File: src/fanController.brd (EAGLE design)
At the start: 41.6 x 36.8 mm, 20 parts, among them Q1 MOSFET-NCHANNELFDD8780

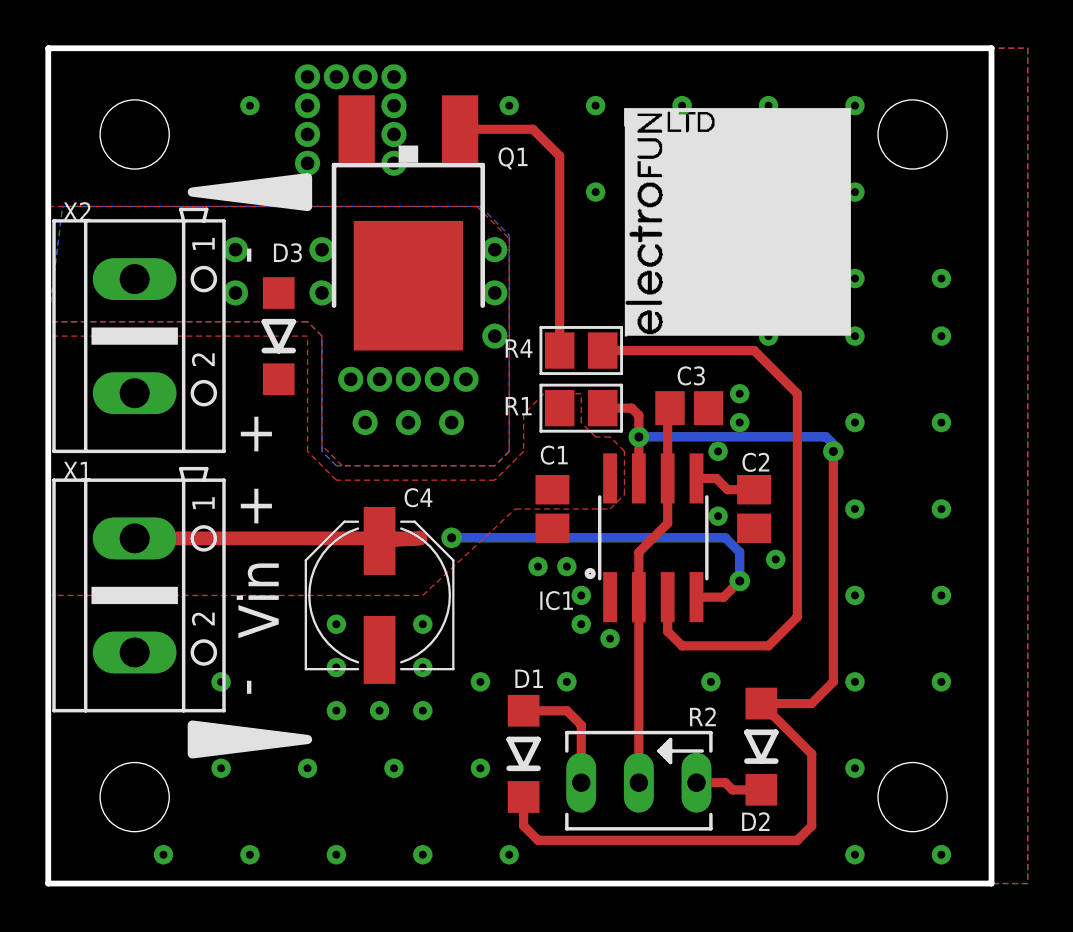
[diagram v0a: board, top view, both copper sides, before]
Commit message: Updated fan controller.
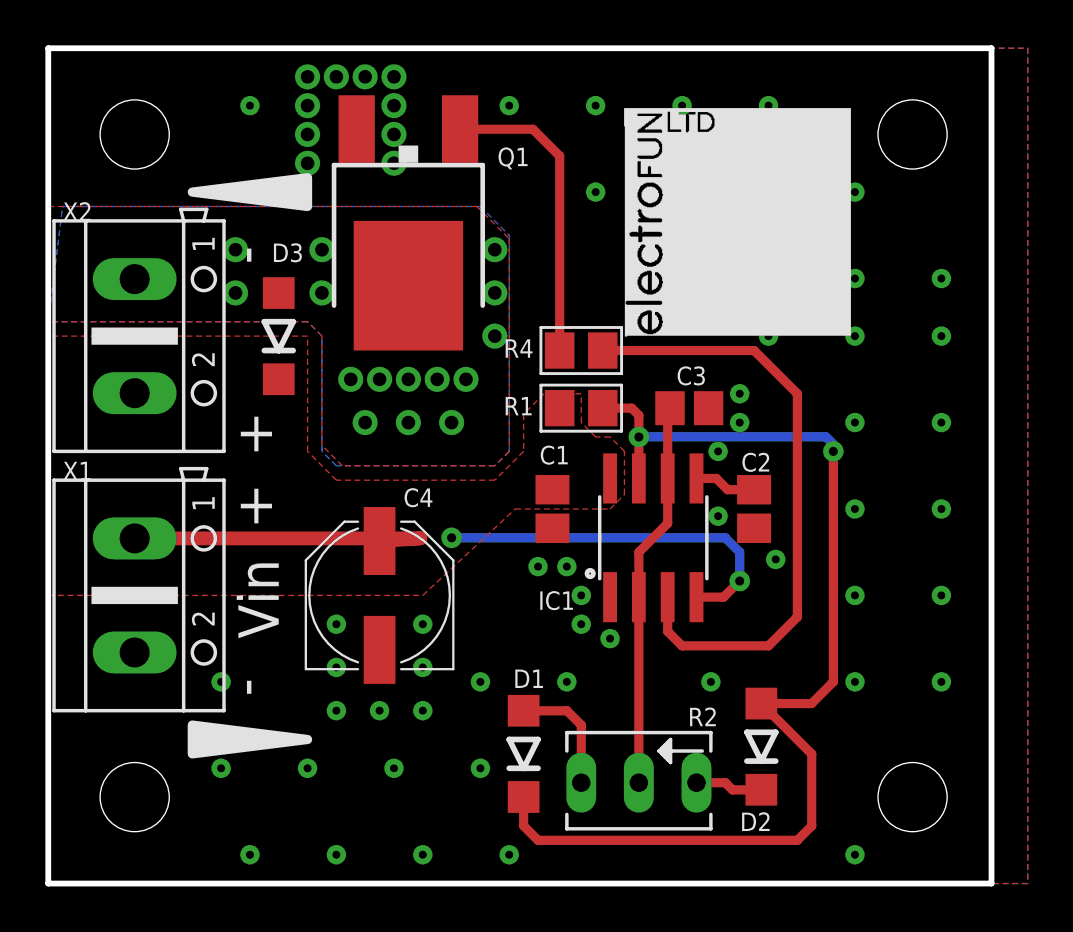
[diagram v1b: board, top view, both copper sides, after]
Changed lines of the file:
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@@
 <layer number="37" name="tTest" color="7" fill="1" visible="no" active="yes"/>
 <layer number="38" name="bTest" color="7" fill="1" visible="no" active="yes"/>
-<layer number="39" name="tKeepout" color="4" fill="11" visible="no" active="yes"/>
-<layer number="40" name="bKeepout" color="1" fill="11" visible="no" active="yes"/>
+<layer number="39" name="tKeepout" color="4" fill="11" visible="yes" active="yes"/>
+<layer number="40" name="bKeepout" color="1" fill="11" visible="yes" active="yes"/>
 <layer number="41" name="tRestrict" color="4" fill="10" visible="no" active="yes"/>
 <layer number="42" name="bRestrict" color="1" fill="10" visible="no" active="yes"/>
@@
 <via x="27.94" y="34.29" extent="1-16" drill="0.35"/>
 <via x="31.75" y="34.29" extent="1-16" drill="0.35"/>
-<via x="35.56" y="34.29" extent="1-16" drill="0.35"/>
 <via x="35.56" y="30.48" extent="1-16" drill="0.35"/>
 <via x="31.75" y="30.48" extent="1-16" drill="0.35"/>
@@
 <via x="20.32" y="1.27" extent="1-16" drill="0.35"/>
 <via x="35.56" y="1.27" extent="1-16" drill="0.35"/>
-<via x="39.37" y="1.27" extent="1-16" drill="0.35"/>
 <via x="20.32" y="34.29" extent="1-16" drill="0.35"/>
 <via x="19.05" y="8.89" extent="1-16" drill="0.35"/>
@@
 <via x="35.56" y="12.7" extent="1-16" drill="0.35"/>
 <via x="35.56" y="8.89" extent="1-16" drill="0.35"/>
-<via x="35.56" y="5.08" extent="1-16" drill="0.35"/>
-<via x="5.08" y="1.27" extent="1-16" drill="0.35"/>
 <via x="7.62" y="8.89" extent="1-16" drill="0.35"/>
 <via x="29.5275" y="16.1925" extent="1-16" drill="0.35"/>

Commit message: Updated final version.
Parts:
- removed R2: 47K, pot:B64Y
- added R3: TSR-3386, SparkFun-Electromechanical:3386U
- moved U$2 2.84 mm to (22.9, 25.4)
- moved D1 1.71 mm to (19.4, 6.35)
- moved D2 1.00 mm to (32.4, 6.35)
- moved R4 0.95 mm to (23.5, 24.4)
- moved C2 0.71 mm to (30.8, 17.1)
- moved Q1 0.32 mm to (15.6, 27.9)
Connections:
- net N$2: now also R3.3; no longer R2.A
- net N$4: now also R3.2; no longer R2.S
- net N$6: now also R3.1; no longer R2.E
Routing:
- net VCC: track 30.8 -> 38.0 mm, vias 2 -> 0
- net CNTRL: track 27.2 -> 28.9 mm
- net N$2: track 5.34 -> 6.86 mm
- net N$6: track 2.99 -> 3.95 mm
- net N$5: track 48.1 -> 49.0 mm, vias 2 -> 0
- net N$3: track 13.5 -> 12.8 mm
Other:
- board size 41.6 x 36.8 mm -> 41.9 x 36.8 mm

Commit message: Updated documentation and layout.
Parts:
- Q1: value MOSFET-NCHANNELFDD8780 -> IPD90N03S4L-03
- R1: value 4K7 -> 1K
- moved D1 3.17 mm to (16.8, 4.45)
- moved D2 2.01 mm to (33.0, 4.45)
- moved U$2 1.93 mm to (24.8, 25.7)
- moved R3 1.27 mm to (24.8, 4.76)
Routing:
- net N$5: track 49.0 -> 52.9 mm
- net N$6: track 3.95 -> 6.64 mm
- net N$2: track 6.86 -> 6.05 mm
- net N$4: track 16.7 -> 17.3 mm

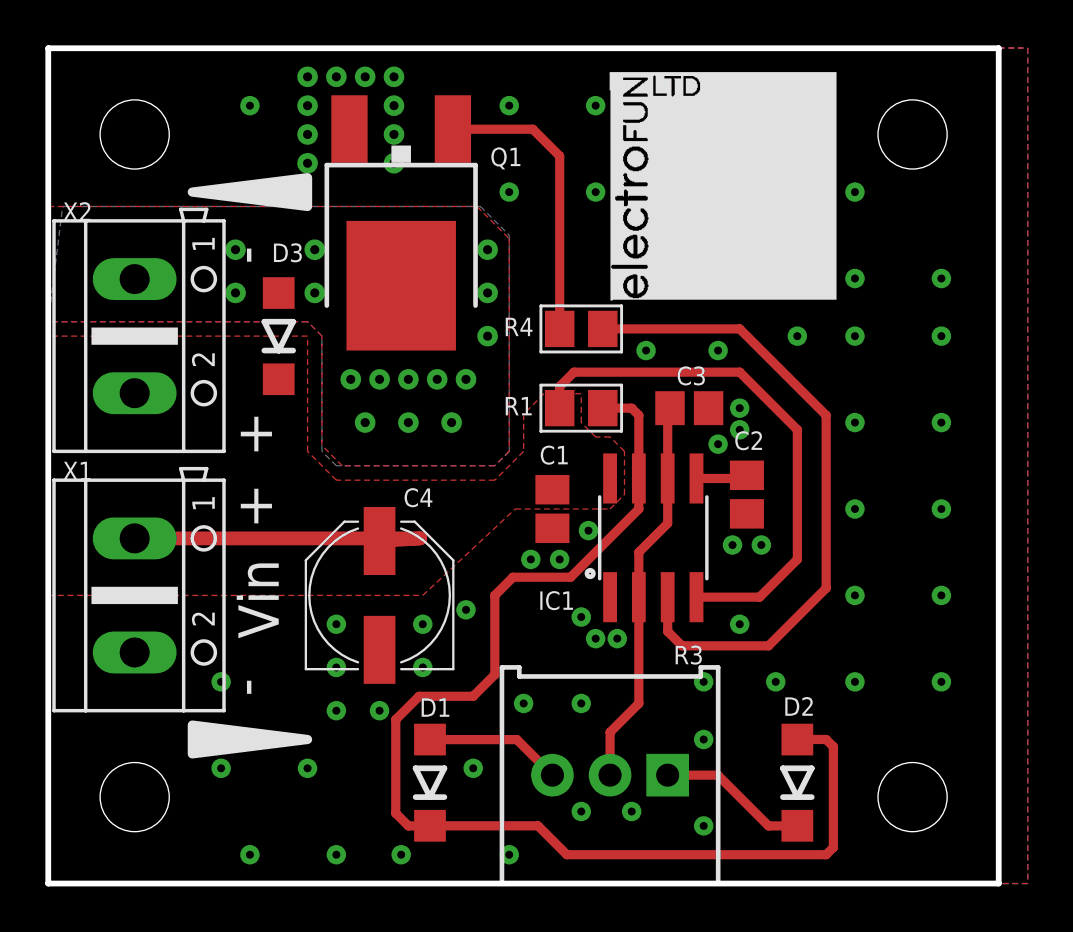
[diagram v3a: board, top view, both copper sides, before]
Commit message: Schematic touchups for final release after testing. Added alternative values to the schematics.
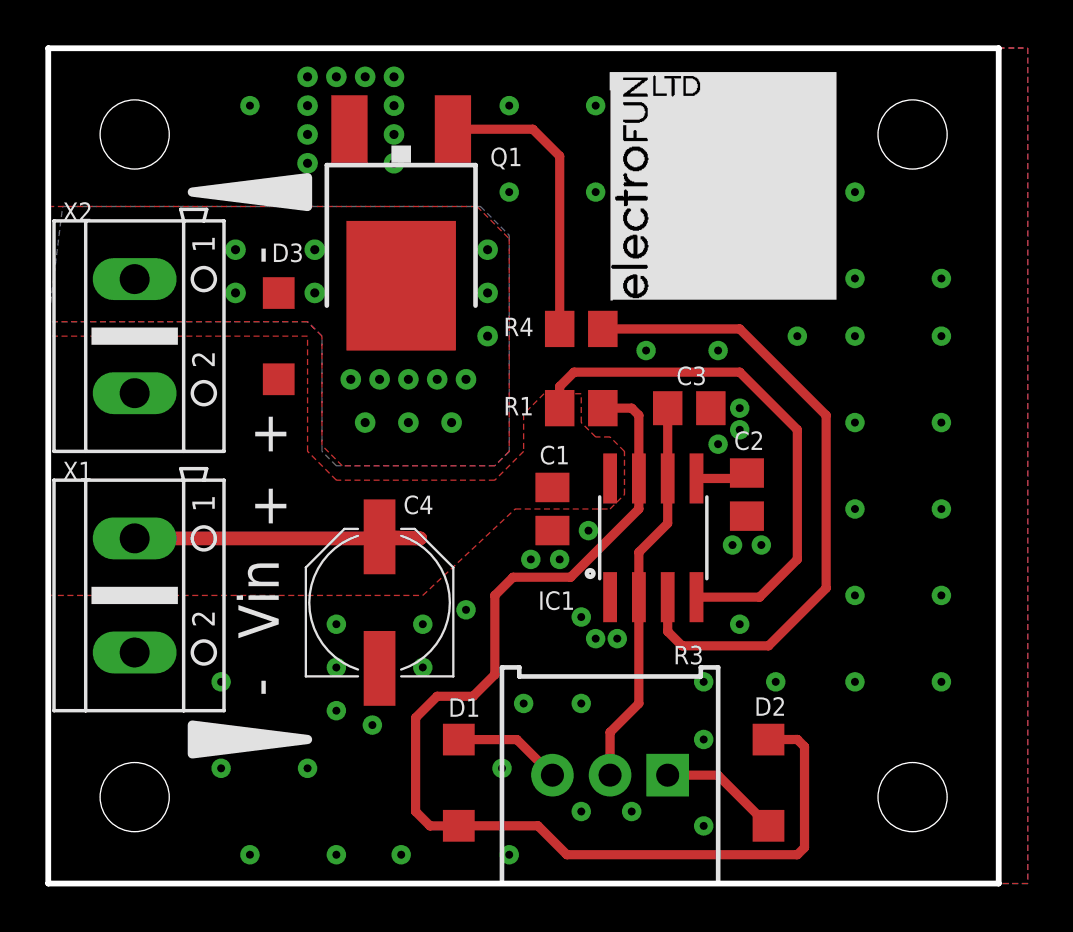
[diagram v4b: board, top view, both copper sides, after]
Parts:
- C3: value 10nF -> 1nF
- R1: value 1K -> 100R
- moved D2 1.27 mm to (31.8, 4.45)
- moved D1 1.27 mm to (18.1, 4.45)
- moved C4 0.32 mm to (14.6, 12.4)
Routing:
- net N$5: track 52.9 -> 49.9 mm
- net N$6: track 6.64 -> 5.37 mm
- net N$2: track 6.05 -> 4.78 mm
